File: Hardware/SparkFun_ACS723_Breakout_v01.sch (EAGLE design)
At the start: 15 parts, among them U1 ACS723ACS723LLCTR-05AB-T2

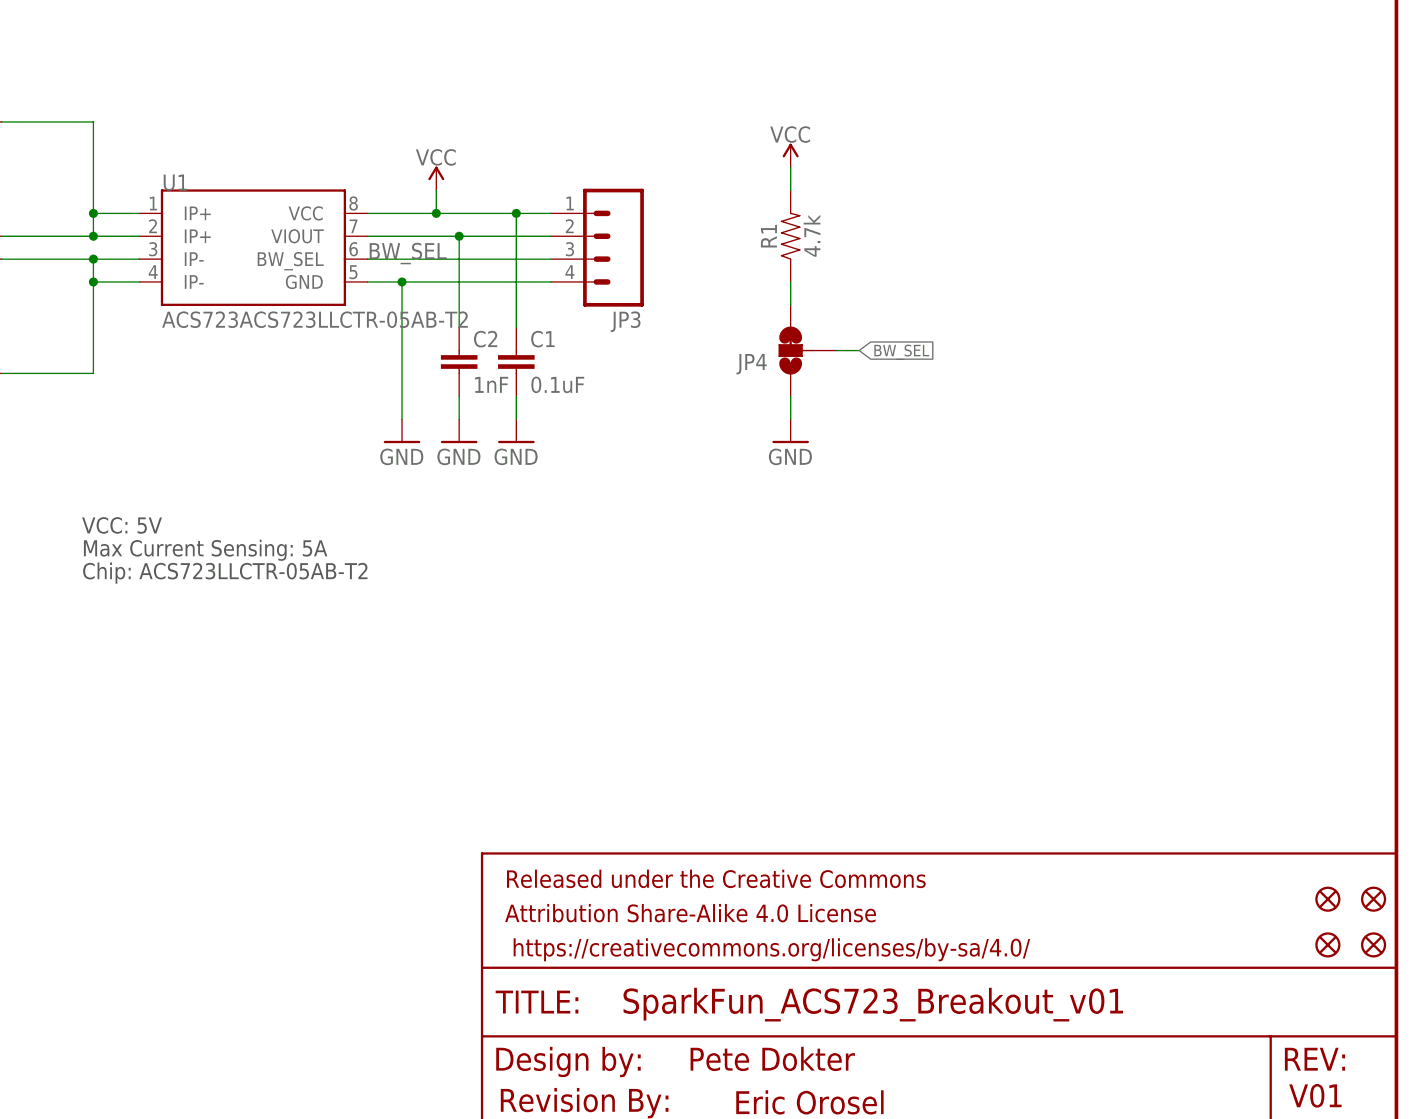
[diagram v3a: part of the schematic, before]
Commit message: Post Eng. Review changes
-added standoff
-removed BW_SEL through-hole
-moved some silk around
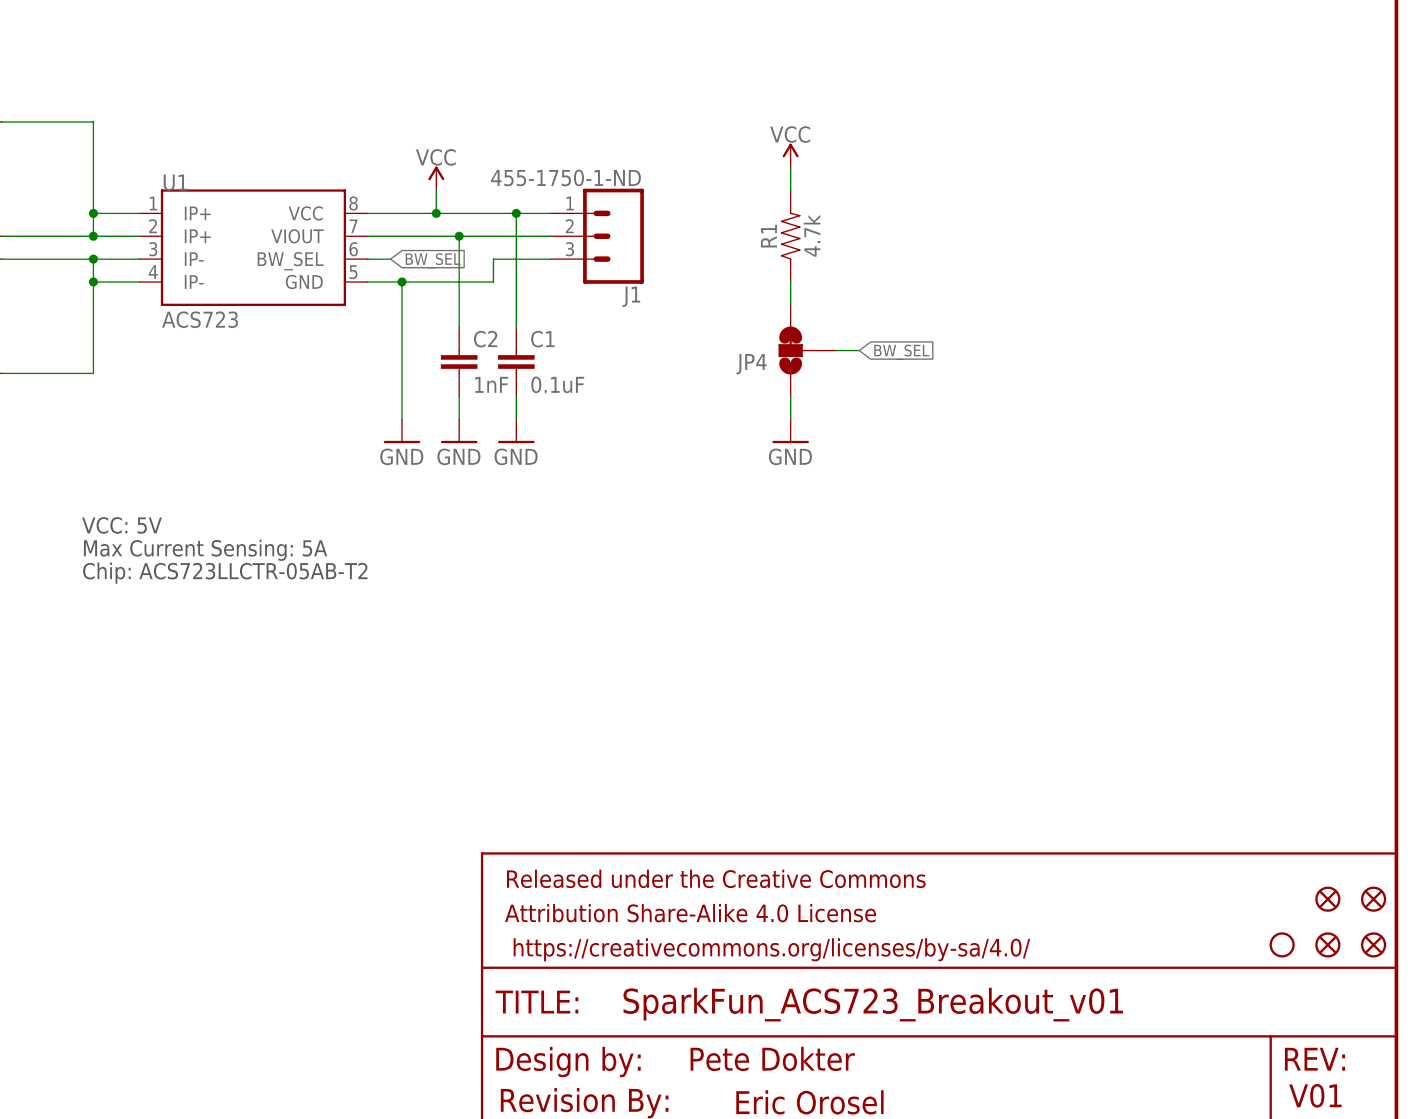
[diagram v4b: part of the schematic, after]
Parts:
- added J1: 455-1750-1-ND, SparkFun-Connectors:CONN_03
- JP3: value (none) -> STAND-OFFTIGHTER_(0.11_INCH_DIA); device SparkFun-Connectors:M04PTH -> Testing:STAND-OFFTIGHTER_(0.11_INCH_DIA)
- U1: value ACS723ACS723LLCTR-05AB-T2 -> ACS723; device SparkFun-IC-Power:ACS723ACS723LLCTR-05AB-T2 -> SparkFun-Sensors:ACS723
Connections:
- net BW_SEL: no longer JP3.3
- net GND: now also J1.3; no longer JP3.4
- net N$1: now also J1.2; no longer JP3.2
- net VCC: now also J1.1; no longer JP3.1
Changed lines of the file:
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@@
 <part name="JP1" library="SparkFun-Connectors" deviceset="M01" device="-SMTSO-256-ET"/>
 <part name="JP2" library="SparkFun-Connectors" deviceset="M01" device="-SMTSO-256-ET"/>
-<part name="JP3" library="SparkFun-Connectors" deviceset="M04" device="PTH"/>
 <part name="JP6" library="SparkFun-Connectors" deviceset="M02" device="1X02_NO_SILK"/>
 <part name="SUPPLY1" library="SparkFun-PowerSymbols" deviceset="VCC" device=""/>
 <part name="GND1" library="SparkFun-Aesthetics" deviceset="GND" device=""/>
 <part name="U$1" library="SparkFun-Aesthetics" deviceset="REVISION" device=""/>
-<part name="U1" library="SparkFun-IC-Power" deviceset="ACS723" device="" technology="ACS723LLCTR-05AB-T2"/>
+<part name="U1" library="SparkFun-Sensors" deviceset="ACS723" device=""/>
 <part name="C1" library="SparkFun-Capacitors" deviceset="0.1UF" device="-0603-25V-(+80/-20%)" value="0.1uF"/>
 <part name="GND2" library="SparkFun-Aesthetics" deviceset="GND" device=""/>
@@
 <part name="GND3" library="SparkFun-Aesthetics" deviceset="GND" device=""/>
 <part name="FRAME1" library="SparkFun-Aesthetics" deviceset="FRAME-LETTER" device=""/>
+<part name="J1" library="SparkFun-Connectors" deviceset="CONN_03" device="" value="455-1750-1-ND"/>
+<part name="JP3" library="Testing" deviceset="STAND-OFF" device="TIGHTER_(0.11_INCH_DIA)"/>
 </parts>
 <sheets>
@@
 <instance part="JP1" gate="G$1" x="86.36" y="116.84"/>
 <instance part="JP2" gate="G$1" x="86.36" y="88.9"/>
-<instance part="JP3" gate="G$1" x="160.02" y="104.14" rot="R180"/>
 <instance part="JP6" gate="G$1" x="86.36" y="101.6"/>
 <instance part="SUPPLY1" gate="G$1" x="142.24" y="109.22"/>
@@
 <instance part="FRAME1" gate="G$1" x="0" y="0"/>
 <instance part="FRAME1" gate="V" x="147.32" y="0"/>
+<instance part="J1" gate="J$1" x="162.56" y="104.14" rot="R180"/>
+<instance part="JP3" gate="G$1" x="236.22" y="25.4"/>
 </instances>
 <busses>
@@
 <pinref part="C1" gate="G$1" pin="1"/>
 <wire x1="151.13" y1="93.98" x2="151.13" y2="106.68" width="0.1524" layer="91"/>
-<pinref part="JP3" gate="G$1" pin="1"/>
 <junction x="142.24" y="106.68"/>
 <pinref part="U1" gate="G$1" pin="VCC"/>
@@
 <junction x="151.13" y="106.68"/>
 <wire x1="142.24" y1="106.68" x2="151.13" y2="106.68" width="0.1524" layer="91"/>
+<pinref part="J1" gate="J$1" pin="1"/>
 </segment>
 <segment>
@@
 <wire x1="138.43" y1="99.06" x2="138.43" y2="83.82" width="0.1524" layer="91"/>
 <pinref part="GND1" gate="1" pin="GND"/>
-<pinref part="JP3" gate="G$1" pin="4"/>
-<wire x1="138.43" y1="99.06" x2="154.94" y2="99.06" width="0.1524" layer="91"/>
+<wire x1="138.43" y1="99.06" x2="148.59" y2="99.06" width="0.1524" layer="91"/>
 <pinref part="U1" gate="G$1" pin="GND"/>
 <wire x1="138.43" y1="99.06" x2="134.62" y2="99.06" width="0.1524" layer="91"/>
 <junction x="138.43" y="99.06"/>
+<wire x1="148.59" y1="99.06" x2="148.59" y2="101.6" width="0.1524" layer="91"/>
+<pinref part="J1" gate="J$1" pin="3"/>
+<wire x1="148.59" y1="101.6" x2="154.94" y2="101.6" width="0.1524" layer="91"/>
 </segment>
 <segment>
@@
 <segment>
 <pinref part="U1" gate="G$1" pin="VIOUT"/>
-<pinref part="JP3" gate="G$1" pin="2"/>
 <wire x1="134.62" y1="104.14" x2="144.78" y2="104.14" width="0.1524" layer="91"/>
 <wire x1="144.78" y1="104.14" x2="154.94" y2="104.14" width="0.1524" layer="91"/>
@@
 <junction x="144.78" y="104.14"/>
 <pinref part="C2" gate="G$1" pin="1"/>
+<pinref part="J1" gate="J$1" pin="2"/>
 </segment>
 </net>
@@
 <segment>
 <pinref part="U1" gate="G$1" pin="BW_SEL"/>
-<pinref part="JP3" gate="G$1" pin="3"/>
-<wire x1="134.62" y1="101.6" x2="154.94" y2="101.6" width="0.1524" layer="91"/>
-<label x="134.62" y="101.6" size="1.778" layer="95"/>
+<wire x1="134.62" y1="101.6" x2="137.16" y2="101.6" width="0.1524" layer="91"/>
+<label x="137.16" y="101.6" size="1.27" layer="95" xref="yes"/>
 </segment>
 <segment>

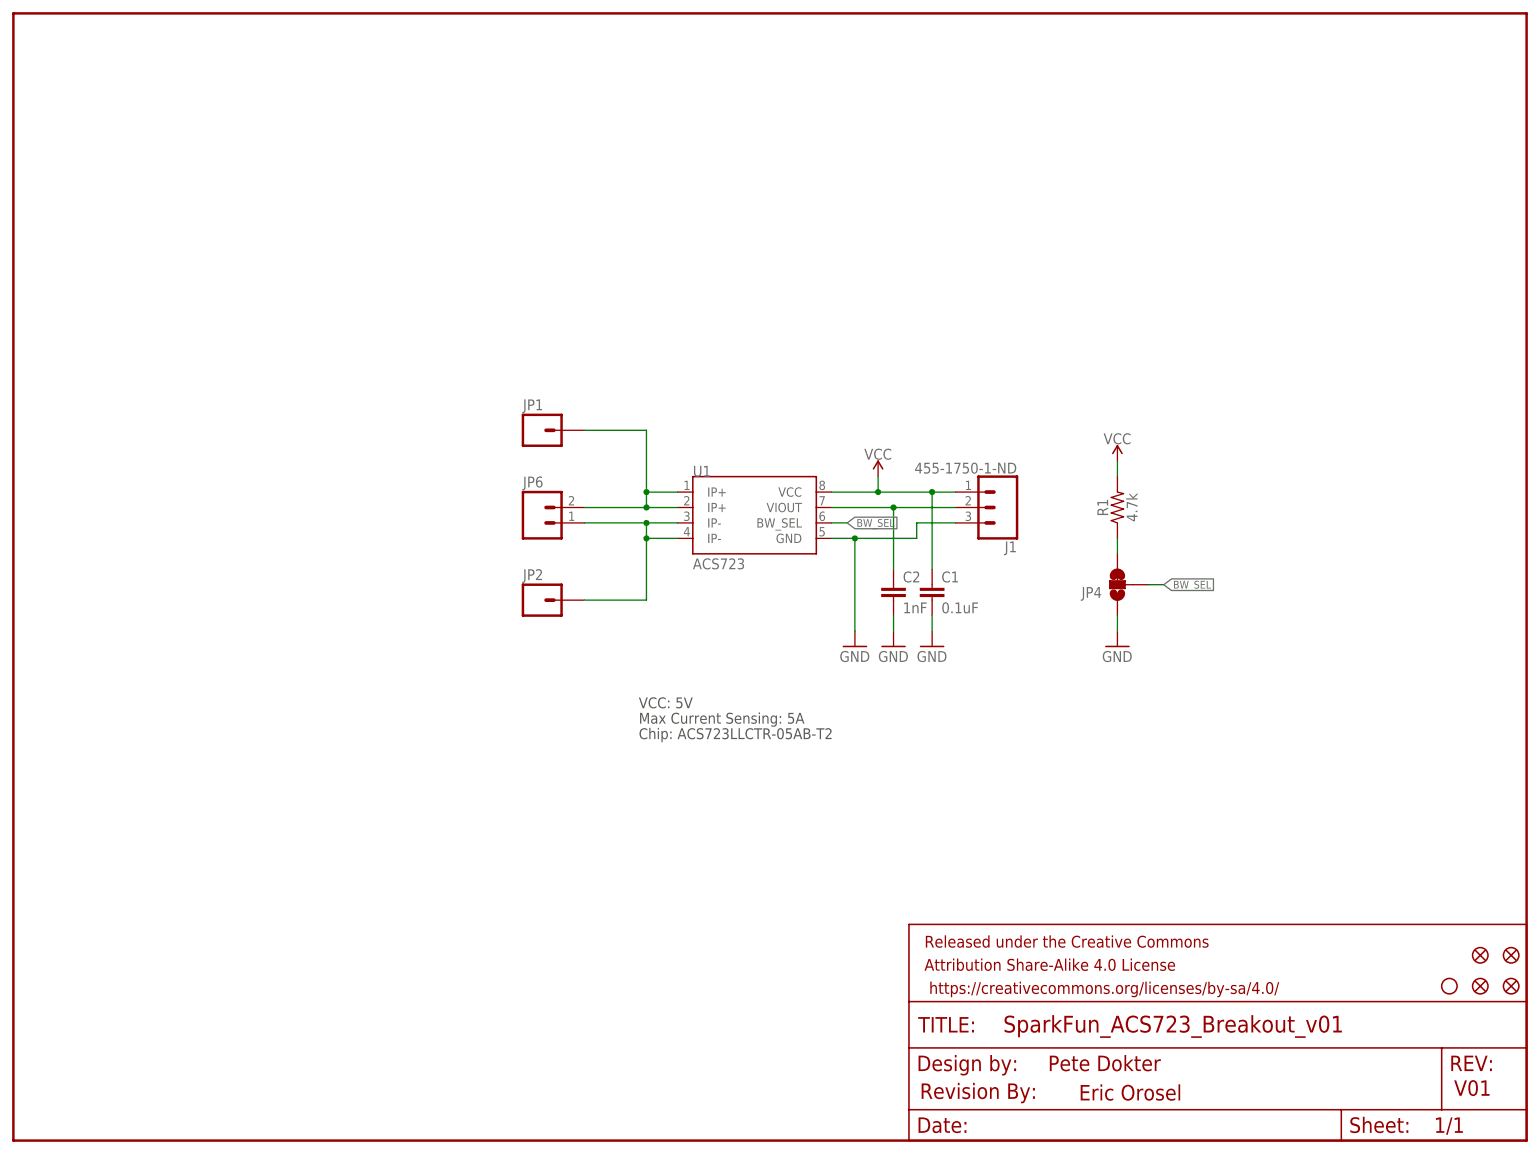
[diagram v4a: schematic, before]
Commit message: final touches for checklist
-moved silk
-moved headers so they're on 100mil grid
- Added measures
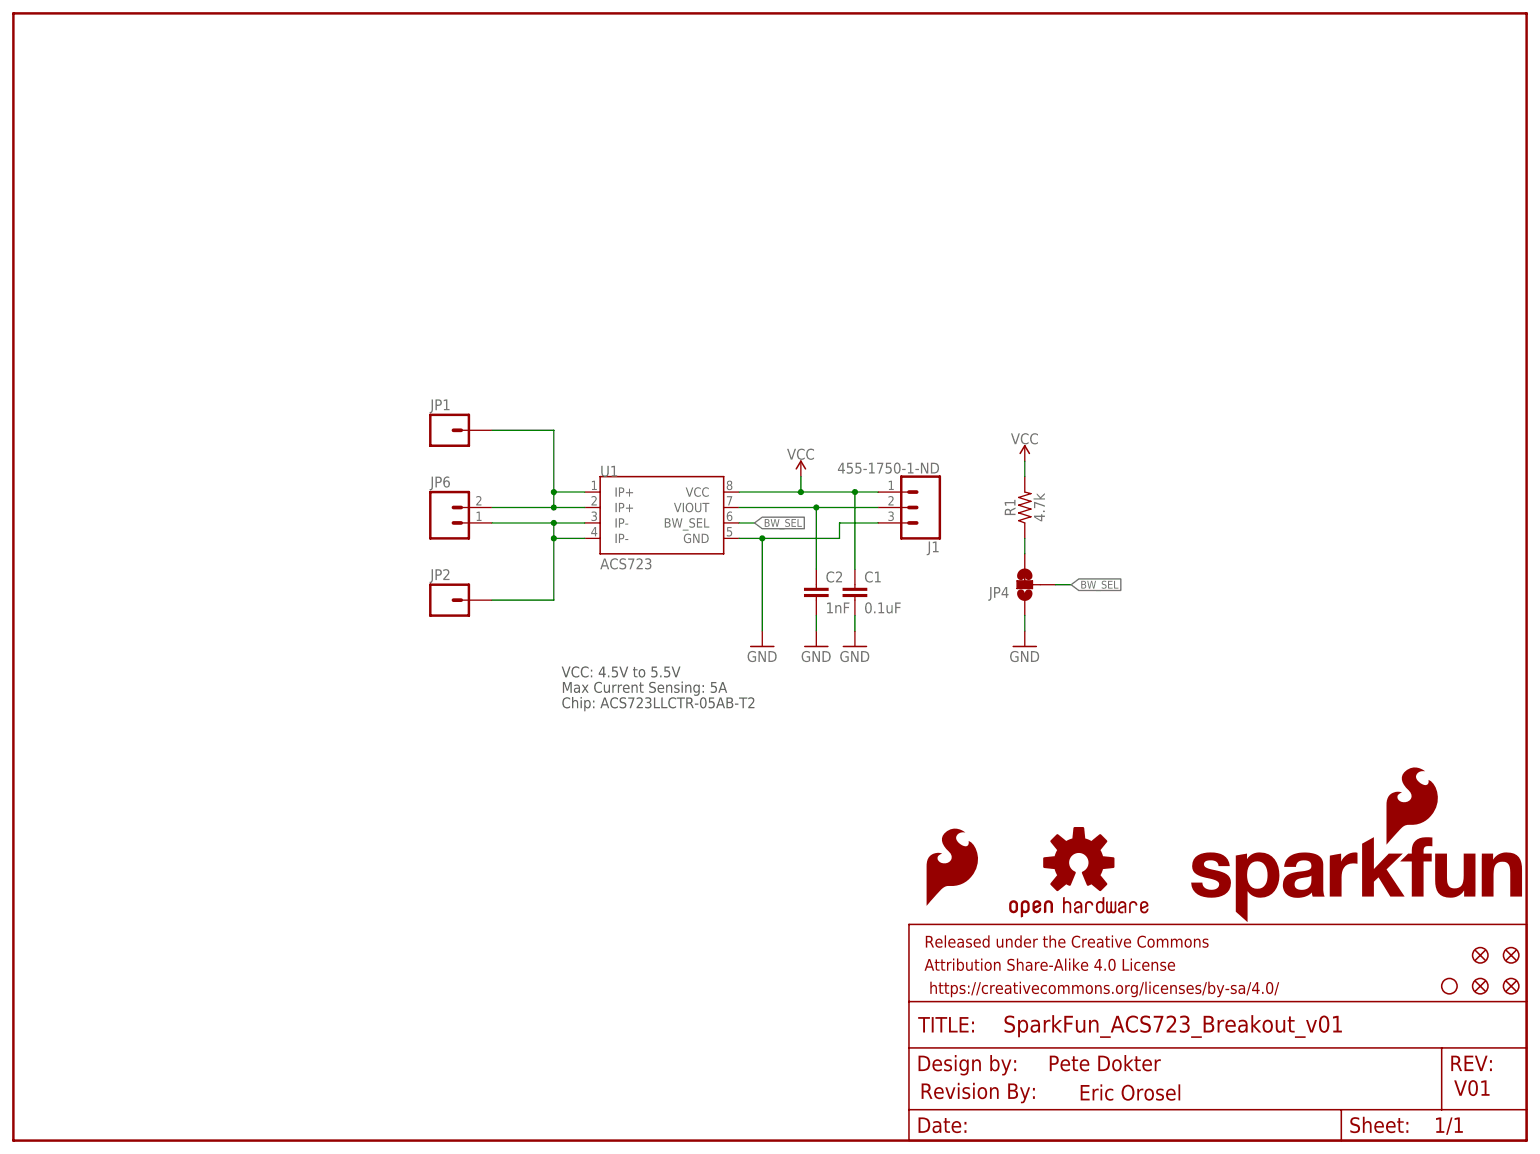
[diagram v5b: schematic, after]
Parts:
- added LOGO1: SFE_LOGO_FLAME.1_INCH, SparkFun-Aesthetics:SFE_LOGO_FLAME.1_INCH
- added LOGO3: SFE_LOGO_NAME_FLAME.1_INCH, SparkFun-Aesthetics:SFE_LOGO_NAME_FLAME.1_INCH
- added LOGO4: OSHW-LOGOM, SparkFun-Aesthetics:OSHW-LOGOM
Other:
- note added: "VCC: 4.5V to 5.5V"
- note removed: "VCC: 5V"
- moved on the sheet: C1, C2, J1, JP1, JP2, JP4, JP6, R1, U1

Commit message: v01 Proto checklist issues fixed
-added BW_SEL note in SCH
-Removed redundant via by GND through-hole
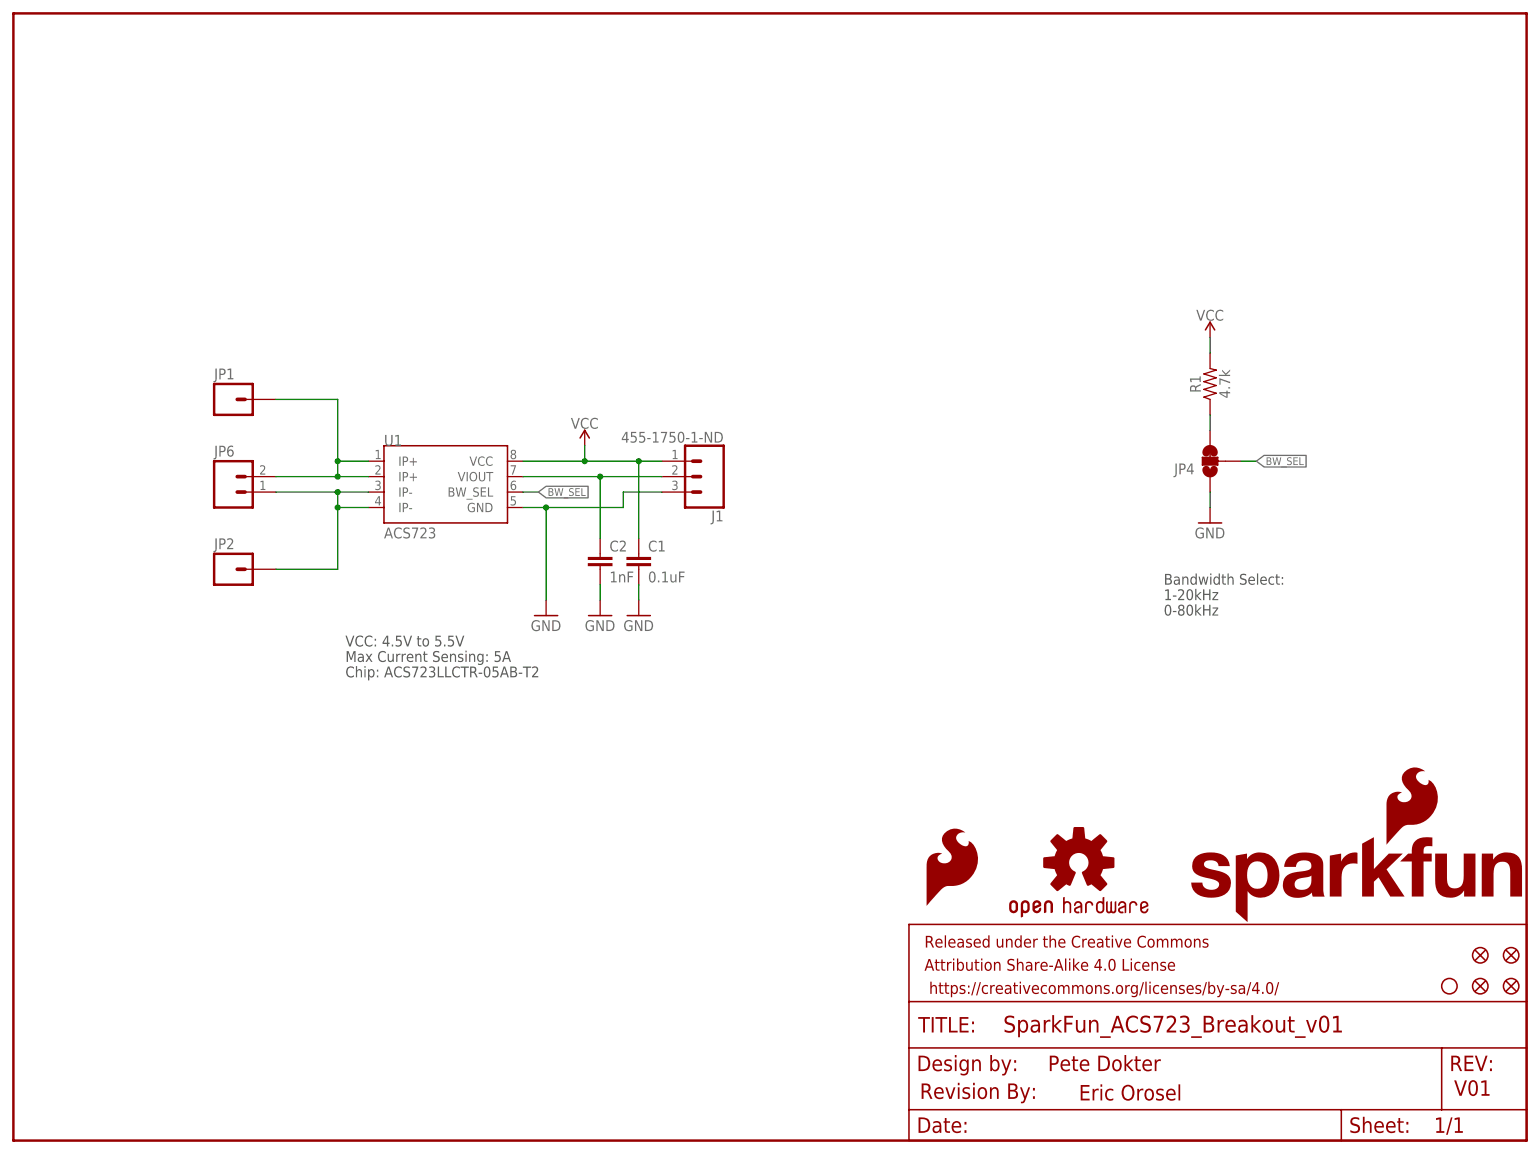
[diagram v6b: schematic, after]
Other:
- note added: "0-80kHz"
- note added: "1-20kHz"
- note added: "Bandwidth Select:"
- moved on the sheet: C1, C2, J1, JP1, JP2, JP4, JP6, R1, U1
